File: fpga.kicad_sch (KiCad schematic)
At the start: 12 parts, among them U11 TLV77512PDBVR, U12 TLV77525PDBVR, U13 TLV77533PDBVR, U2 ICE40LP1K-CM36

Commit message: More re-layout for the new design
Signed-off-by: Corey Minyard <corey@minyard.net>
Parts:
- added R34, R35, R36: 10K, Resistor_SMD:R_0402_1005Metric, symbol Device:R
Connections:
- net +3.3V: now also U11.3 (ON/~{OFF}), R36.2
- net 144MHz_TX_ENABLE: now also U2.A1 (IOL_2B)
- net 144_SWITCH: now also U2.A2 (IOT_89)
- net 440MHz_TX_ENABLE: now also U2.B5 (IOR_63)
- net 440_SWITCH: now also U2.B4 (IOR_61_GBIN2)
- net FPGA_3.3V: now also R35.2
- net FPGA_SPI_SSEL: now also U2.D5 (IOB_47_SS), R34.2
- net GND: now also R34.1
- net RADIO2_RESET_N: now also U2.B6 (IOR_64)
- net RADIO_SPI_MISO: now also U2.E4 (IOB_44_SDO)
- net RADIO_SPI_MOSI: now also U2.F5 (IOB_45_SDI)
- net RADIO_SPI_SCLK: now also U2.E5 (IOB_46_SCK)
- net TX_144_ON: now also U2.A3 (IOT_84_GBIN1)
- net TX_440_ON: now also U2.B3 (IOT_85_GBIN0)
- net RADIO1_GPIO0: now reaches U2.B1 (IOL_2A)
- net RADIO1_GPIO2: now reaches U2.C1 (IOL_6B_GBIN7)
- net FPGA_CDONE/IRQ_N: now reaches U2.C3 (IOT_90)
- net FPGA_CDONE/IRQ_N: now also U2.C4 (CDONE), R36.1
- net RADIO2_GPIO3: now reaches U2.C6 (IOR_65)
- net RADIO1_GPIO3: now reaches U2.D1 (IOL_7A_GBIN6)
- net RADIO2_GPIO2: now reaches U2.D6 (IOR_55)
- net RADIO1_RESET_N: now reaches U2.E1 (IOL_7B)
- net RADIO2_GPIO0: now reaches U2.E6 (IOR_54)
- net FPGA_RESET_N: now reaches U2.F4 (CRESET_B)
- net FPGA_RESET_N: now also R35.1
- no-connect marks 2 -> 7
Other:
- moved on the sheet: U2

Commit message: Finish initial layet
Signed-off-by: Corey Minyard <corey@minyard.net>
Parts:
- added R37, R38: 0, Resistor_SMD:R_0402_1005Metric, symbol Device:R
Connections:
- net at U2.C2 (IOL_6A): now also R37.2
- net at U2.F3 (IOB_43_CBSEL1): now also R38.2
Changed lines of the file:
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@@
-	)
-	(no_connect
-		(at 187.96 49.53)
 	)
 	(no_connect
@@
 	)
 	(no_connect
+		(at 240.03 95.25)
+	)
+	(no_connect
+		(at 240.03 49.53)
+	)
+	(no_connect
 		(at 187.96 64.77)
 	)
@@
 		(at 96.52 44.45)
 	)
-	(no_connect
-		(at 187.96 95.25)
-	)
 	(wire
 		(pts
@@
 	(wire
 		(pts
+			(xy 187.96 49.53) (xy 232.41 49.53)
+		)
+		(stroke
+			(width 0)
+			(type default)
+		)
+	)
+	(wire
+		(pts
 			(xy 187.96 57.15) (xy 208.28 57.15)
 		)
@@
 		(pts
 			(xy 20.32 67.31) (xy 20.32 137.16)
+		)
+		(stroke
+			(width 0)
+			(type default)
+		)
+	)
+	(wire
+		(pts
+			(xy 187.96 95.25) (xy 232.41 95.25)
 		)
 		(stroke
@@
 	)
 	(symbol
+		(lib_id "Device:R")
+		(at 236.22 49.53 270)
+		(unit 1)
+		(exclude_from_sim no)
+		(in_bom no)
+		(on_board yes)
+		(dnp yes)
+		(property "Reference" "R38"
+			(at 241.046 51.054 90)
+			(effects
+				(font
+					(size 1.27 1.27)
+				)
+			)
+		)
+		(property "Value" "0"
+			(at 232.156 50.546 90)
+			(effects
+				(font
+					(size 1.27 1.27)
+				)
+			)
+		)
+		(property "Footprint" "Resistor_SMD:R_0402_1005Metric"
+			(at 236.22 47.752 90)
+			(effects
+				(font
+					(size 1.27 1.27)
+				)
+				(hide yes)
+			)
+		)
+		(property "Datasheet" "~"
+			(at 236.22 49.53 0)
+			(effects
+				(font
+					(size 1.27 1.27)
+				)
+				(hide yes)
+			)
+		)
+		(property "Description" "Resistor"
+			(at 236.22 49.53 0)
+			(effects
+				(font
+					(size 1.27 1.27)
+				)
+				(hide yes)
+			)
+		)
+		(pin "2"
+		)
+		(pin "1"
+		)
+		(instances
+			(project "FSKGroundStation"
+				(path "/23e49ab9-97e0-460a-806c-ff6f37958474/a7d34897-eb3f-4db7-9b4e-9397ce1d9e5d"
+					(reference "R38")
+					(unit 1)
+				)
+			)
+		)
+	)
+	(symbol
 		(lib_id "Local ICs:TLV775 3.3V")
 		(at 45.72 100.33 0)
@@
 		(on_board yes)
 		(dnp no)
-		(fields_autoplaced yes)
 		(property "Reference" "#PWR0147"
 			(at 236.22 92.71 0)
@@
 		)
 		(property "Value" "GND"
-			(at 236.22 91.44 0)
+			(at 236.22 90.17 0)
 			(effects
 				(font
@@
 					(unit 1)
 				)
+			)
+		)
+	)
+	(symbol
+		(lib_id "Device:R")
+		(at 236.22 95.25 270)
+		(unit 1)
+		(exclude_from_sim no)
+		(in_bom no)
+		(on_board yes)
+		(dnp yes)
+		(property "Reference" "R37"
+			(at 236.474 98.044 90)
+			(effects
+				(font
+					(size 1.27 1.27)
+				)
+			)
+		)
+		(property "Value" "0"
+			(at 236.22 92.71 90)
+			(effects
+				(font
+					(size 1.27 1.27)
+				)
+			)
+		)
+		(property "Footprint" "Resistor_SMD:R_0402_1005Metric"
+			(at 236.22 93.472 90)
+			(effects
+				(font
+					(size 1.27 1.27)
+				)
+				(hide yes)
+			)
+		)
+		(property "Datasheet" "~"
+			(at 236.22 95.25 0)
+			(effects
+				(font
+					(size 1.27 1.27)
+				)
+				(hide yes)
+			)
+		)
+		(property "Description" "Resistor"
+			(at 236.22 95.25 0)
+			(effects
+				(font
+					(size 1.27 1.27)
+				)
+				(hide yes)
+			)
+		)
+		(pin "2"
+		)
+		(pin "1"
+		)
+		(instances
+			(project "FSKGroundStation"
+				(path "/23e49ab9-97e0-460a-806c-ff6f37958474/a7d34897-eb3f-4db7-9b4e-9397ce1d9e5d"
+					(reference "R37")
+					(unit 1)
+				)

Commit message: Add some LEDs
Signed-off-by: Corey Minyard <corey@minyard.net>
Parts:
- added D3: RED LED, LED_SMD:LED_0603_1608Metric_Pad1.05x0.95mm_HandSolder, symbol Device:LED
- added D5: GREEN LED, LED_SMD:LED_0603_1608Metric_Pad1.05x0.95mm_HandSolder, symbol Device:LED
- R37, R38: value 0 -> 3KΩ; footprint Resistor_SMD:R_0402_1005Metric -> Resistor_SMD:R_0603_1608Metric_Pad0.98x0.95mm_HandSolder; now fitted; now in the parts list
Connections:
- net +3.3V: now also D3.2 (A), D5.2 (A)
- net at R38.1: now also D5.1 (K)
- net at R37.1: now also D3.1 (K)
- no-connect marks 7 -> 5

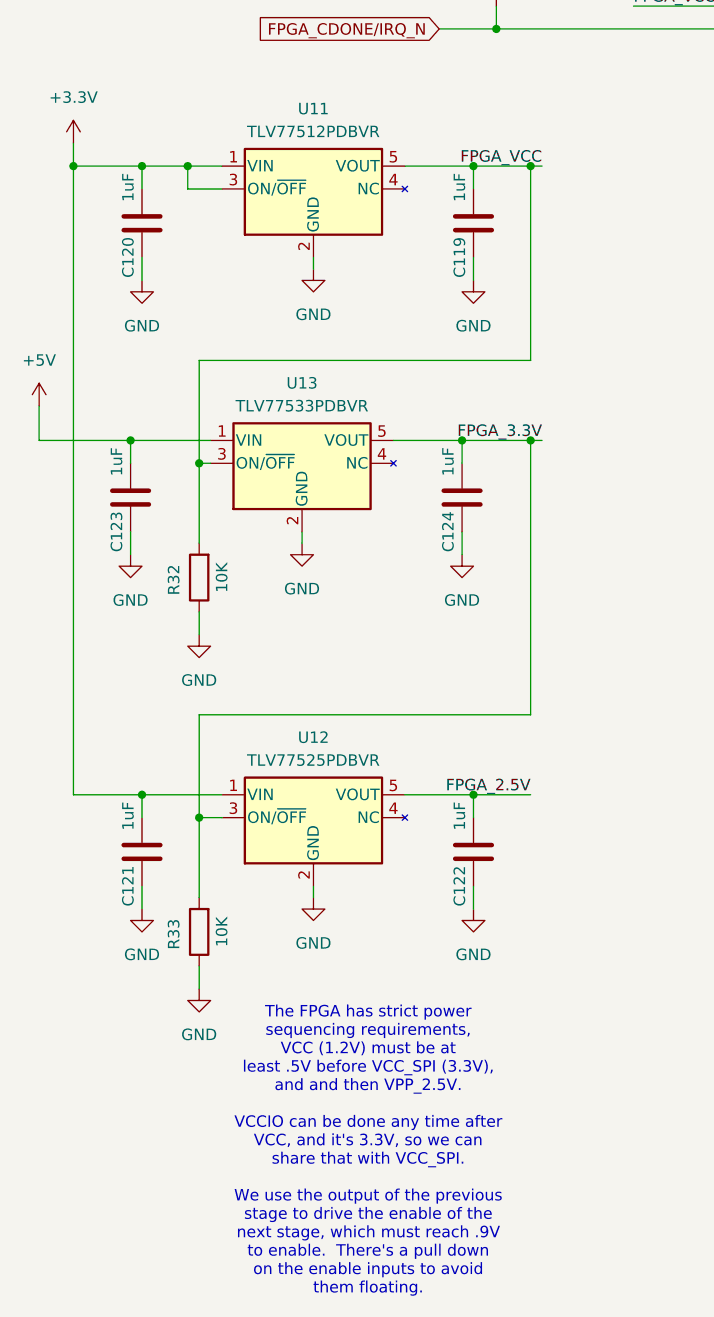
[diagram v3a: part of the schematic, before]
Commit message: Use a diode to provide the 2.5V voltage for the FPGA
Drops 3.3V down to 2.8V, which is in range.  It's a lot simpler.

Also do some via cleanup.

Signed-off-by: Corey Minyard <corey@minyard.net>
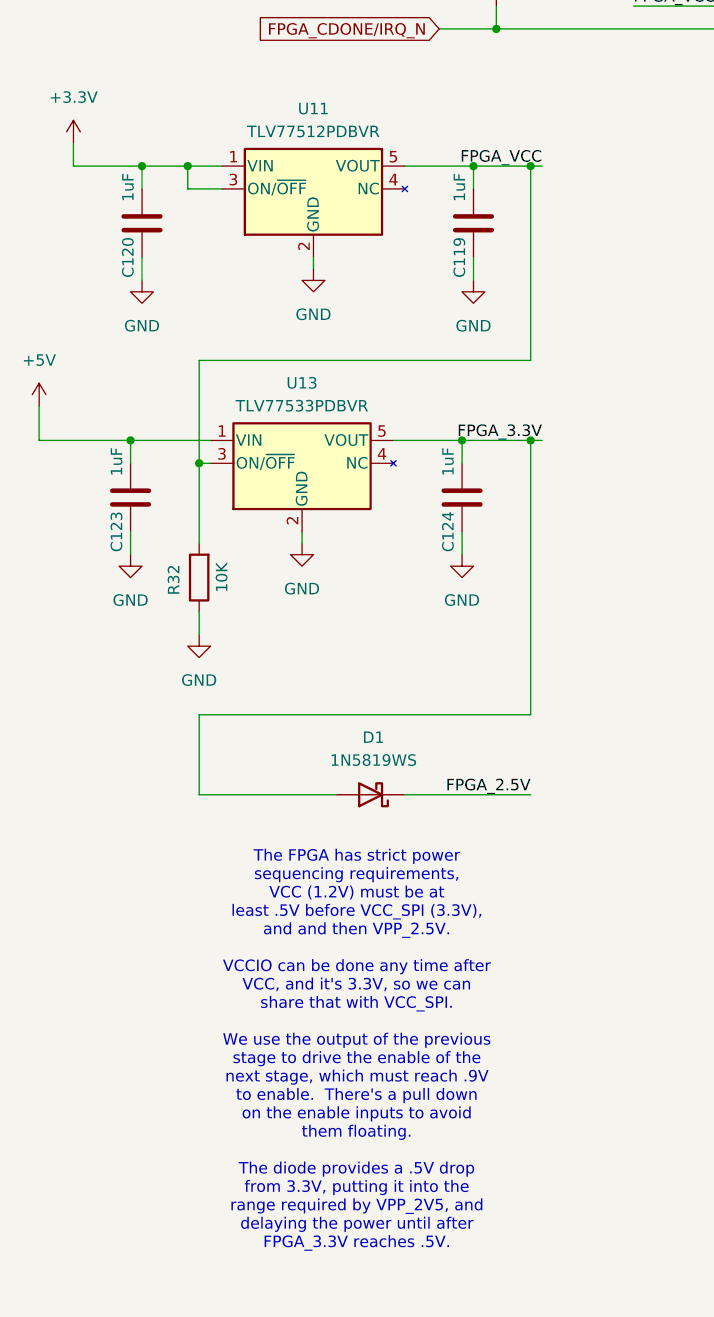
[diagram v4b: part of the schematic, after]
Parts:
- removed C121, C122: 1uF, Capacitor_SMD:C_0603_1608Metric_Pad1.08x0.95mm_HandSolder, symbol Device:C
- removed R33: 10K, Resistor_SMD:R_0402_1005Metric, symbol Device:R
- removed U12: TLV77525PDBVR, Package_TO_SOT_SMD:SOT-23-5, symbol Local ICs:TLV775 2.5V
- added D1: 1N5819WS, Diode_SMD:D_SOD-323, symbol Diode:1N5819WS
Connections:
- net FPGA_2.5V: now also D1.1 (K)
- net FPGA_3.3V: now also D1.2 (A)
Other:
- note added: "The FPGA has strict power sequencing requirements, VCC (1.2V) must be at least .5V before VCC_SPI (3.3V), and and then VPP_2.5V. VCCIO can be done any time after VCC, and it's 3.3V, so we can share that with VCC_SPI. We use the output of the previous stage to drive the enable of the next stage, which must reach .9V to enable. There's a pull down on the enable inputs to avoid them floating. The di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"
- note removed: "The FPGA has strict power sequencing requirements, VCC (1.2V) must be at least .5V before VCC_SPI (3.3V), and and then VPP_2.5V. VCCIO can be done any time after VCC, and it's 3.3V, so we can share that with VCC_SPI. We use the output of the previous stage to drive the enable of the next stage, which must reach .9V to enable. There's a pull down on the enable inputs to avoid them floating."

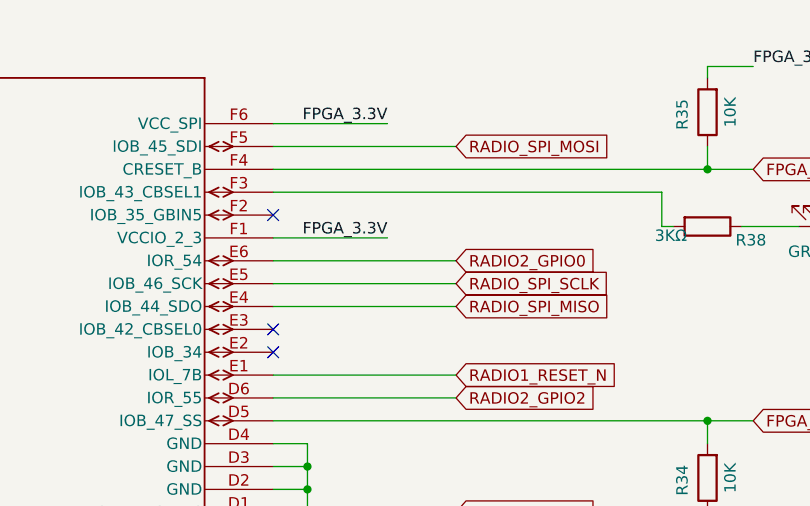
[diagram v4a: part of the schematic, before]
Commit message: Add a DNP resistor on an FPGA pin
Make it available for use.  Clean up routing around the FPGA a bit, too.

Signed-off-by: Corey Minyard <corey@minyard.net>
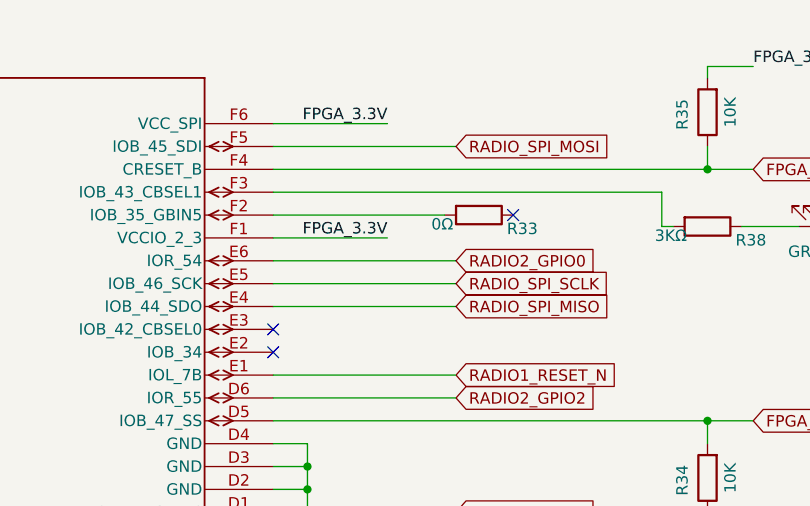
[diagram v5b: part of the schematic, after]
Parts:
- added R33: 0Ω, Resistor_SMD:R_0402_1005Metric_Pad0.72x0.64mm_HandSolder, symbol Device:R
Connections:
- net at U2.F2 (IOB_35_GBIN5): now also R33.2
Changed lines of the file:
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@@
-	)
-	(no_connect
-		(at 187.96 52.07)
 	)
 	(no_connect
@@
 	)
 	(no_connect
+		(at 214.63 52.07)
+	)
+	(no_connect
 		(at 187.96 64.77)
 	)
@@
 		(pts
 			(xy 34.29 128.27) (xy 34.29 137.16)
+		)
+		(stroke
+			(width 0)
+			(type default)
+		)
+	)
+	(wire
+		(pts
+			(xy 187.96 52.07) (xy 207.01 52.07)
 		)
 		(stroke
@@
 					(unit 1)
 				)
+			)
+		)
+	)
+	(symbol
+		(lib_id "Device:R")
+		(at 210.82 52.07 270)
+		(unit 1)
+		(exclude_from_sim no)
+		(in_bom yes)
+		(on_board yes)
+		(dnp no)
+		(property "Reference" "R33"
+			(at 215.646 53.594 90)
+			(effects
+				(font
+					(size 1.27 1.27)
+				)
+			)
+		)
+		(property "Value" "0Ω"
+			(at 206.756 53.086 90)
+			(effects
+				(font
+					(size 1.27 1.27)
+				)
+			)
+		)
+		(property "Footprint" "Resistor_SMD:R_0402_1005Metric_Pad0.72x0.64mm_HandSolder"
+			(at 210.82 50.292 90)
+			(effects
+				(font
+					(size 1.27 1.27)
+				)
+				(hide yes)
+			)
+		)
+		(property "Datasheet" "~"
+			(at 210.82 52.07 0)
+			(effects
+				(font
+					(size 1.27 1.27)
+				)
+				(hide yes)
+			)
+		)
+		(property "Description" "Resistor"
+			(at 210.82 52.07 0)
+			(effects
+				(font
+					(size 1.27 1.27)
+				)
+				(hide yes)
+			)
+		)
+		(pin "2"
+		)
+		(pin "1"
+		)
+		(instances
+			(project "FSKGroundStation"
+				(path "/23e49ab9-97e0-460a-806c-ff6f37958474/a7d34897-eb3f-4db7-9b4e-9397ce1d9e5d"
+					(reference "R33")
+					(unit 1)
+				)

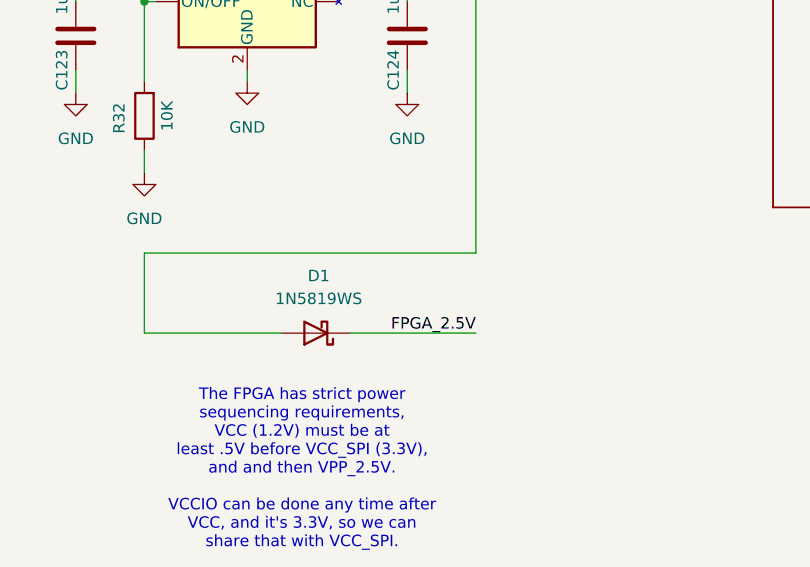
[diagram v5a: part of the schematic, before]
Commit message: Switch to a CPU with a USB interface for the USB connection
The part that was picked had proprietary tools and configuration and it
didn't support interrupts.  The CPU is cheaper and more capable.

Signed-off-by: Corey Minyard <corey@minyard.net>
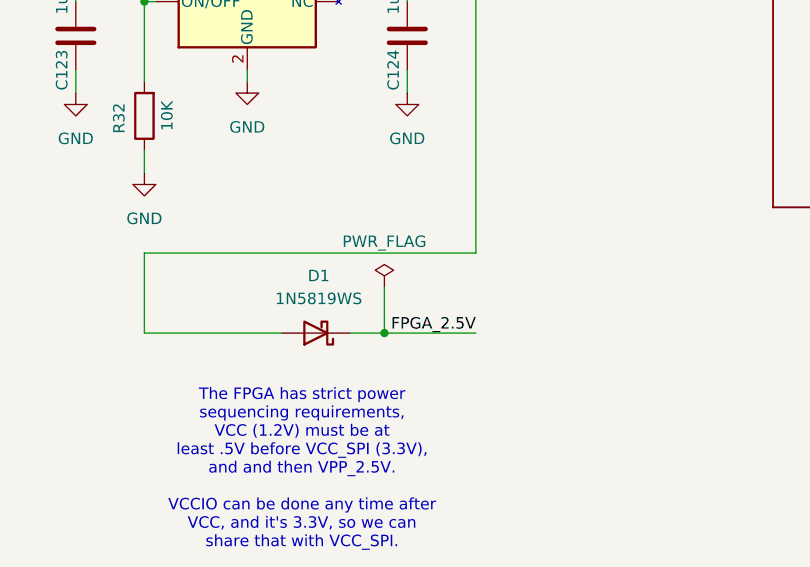
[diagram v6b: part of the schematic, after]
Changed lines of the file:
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@@
+	)
+	(junction
+		(at 60.96 137.16)
+		(diameter 0)
+		(color 0 0 0 0)
 	)
 	(junction
@@
 	(wire
 		(pts
-			(xy 57.15 137.16) (xy 71.12 137.16)
+			(xy 57.15 137.16) (xy 60.96 137.16)
 		)
 		(stroke
@@
 		(pts
 			(xy 82.55 41.91) (xy 96.52 41.91)
+		)
+		(stroke
+			(width 0)
+			(type default)
+		)
+	)
+	(wire
+		(pts
+			(xy 60.96 137.16) (xy 71.12 137.16)
+		)
+		(stroke
+			(width 0)
+			(type default)
+		)
+	)
+	(wire
+		(pts
+			(xy 60.96 132.08) (xy 60.96 137.16)
 		)
 		(stroke
@@
 					(unit 1)
 				)
+			)
+		)
+	)
+	(symbol
+		(lib_id "power:PWR_FLAG")
+		(at 60.96 132.08 0)
+		(unit 1)
+		(exclude_from_sim no)
+		(in_bom yes)
+		(on_board yes)
+		(dnp no)
+		(fields_autoplaced yes)
+		(property "Reference" "#FLG05"
+			(at 60.96 130.175 0)
+			(effects
+				(font
+					(size 1.27 1.27)
+				)
+				(hide yes)
+			)
+		)
+		(property "Value" "PWR_FLAG"
+			(at 60.96 127 0)
+			(effects
+				(font
+					(size 1.27 1.27)
+				)
+			)
+		)
+		(property "Footprint" ""
+			(at 60.96 132.08 0)
+			(effects
+				(font
+					(size 1.27 1.27)
+				)
+				(hide yes)
+			)
+		)
+		(property "Datasheet" "~"
+			(at 60.96 132.08 0)
+			(effects
+				(font
+					(size 1.27 1.27)
+				)
+				(hide yes)
+			)
+		)
+		(property "Description" "Special symbol for telling ERC where power comes from"
+			(at 60.96 132.08 0)
+			(effects
+				(font
+					(size 1.27 1.27)
+				)
+				(hide yes)
+			)
+		)
+		(pin "1"
+		)
+		(instances
+			(project "FSKGroundStation"
+				(path "/23e49ab9-97e0-460a-806c-ff6f37958474/a7d34897-eb3f-4db7-9b4e-9397ce1d9e5d"
+					(reference "#FLG05")
+					(unit 1)
+				)

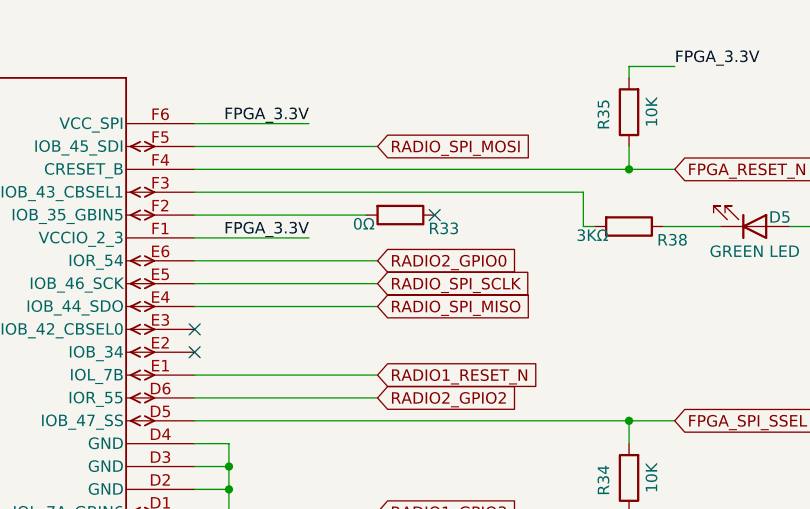
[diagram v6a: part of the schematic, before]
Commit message: Add a clock from the USB chip to the FPGA
The FPGA might need a clock for certain things, so provide it.

Signed-off-by: Corey Minyard <corey@minyard.net>
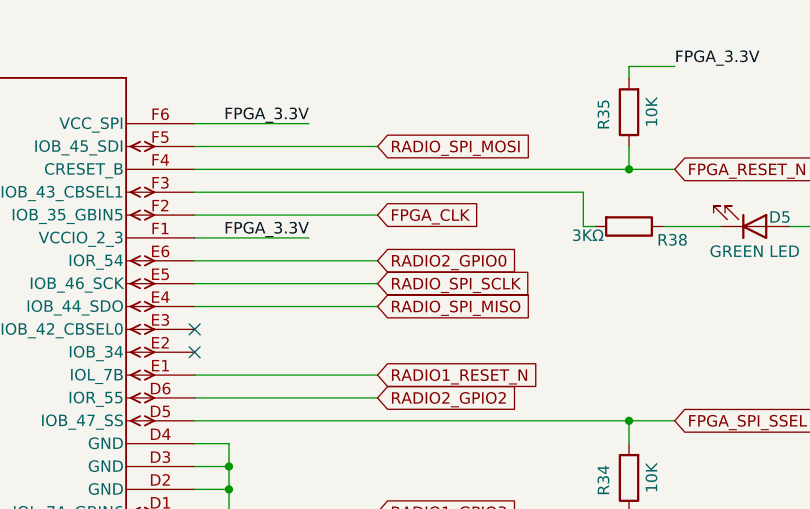
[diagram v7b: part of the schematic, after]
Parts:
- removed R33: 0Ω, Resistor_SMD:R_0402_1005Metric_Pad0.72x0.64mm_HandSolder, symbol Device:R
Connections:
- net FPGA_CLK: now reaches U2.F2 (IOB_35_GBIN5)
- no-connect marks 5 -> 4
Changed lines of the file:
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@@
-	)
-	(no_connect
-		(at 214.63 52.07)
 	)
 	(no_connect
@@
 	(wire
 		(pts
-			(xy 187.96 52.07) (xy 207.01 52.07)
+			(xy 187.96 52.07) (xy 208.28 52.07)
 		)
 		(stroke
@@
 		(property "Intersheetrefs" "${INTERSHEET_REFS}"
 			(at 258.618 74.93 0)
+			(effects
+				(font
+					(size 1.27 1.27)
+				)
+				(justify left)
+				(hide yes)
+			)
+		)
+	)
+	(global_label "FPGA_CLK"
+		(shape input)
+		(at 208.28 52.07 0)
+		(fields_autoplaced yes)
+		(effects
+			(font
+				(size 1.27 1.27)
+			)
+			(justify left)
+		)
+		(property "Intersheetrefs" "${INTERSHEET_REFS}"
+			(at 220.5181 52.07 0)
 			(effects
 				(font
@@
 		)
 		(property "Value" "3KΩ"
-			(at 232.156 54.356 90)
+			(at 231.648 54.356 90)
 			(effects
 				(font
@@
 					(unit 1)
 				)
-			)
-		)
-	)
-	(symbol
-		(lib_id "Device:R")
-		(at 210.82 52.07 270)
-		(unit 1)
-		(exclude_from_sim no)
-		(in_bom yes)
-		(on_board yes)
-		(dnp no)
-		(property "Reference" "R33"
-			(at 215.646 53.594 90)
-			(effects
-				(font
-					(size 1.27 1.27)
-				)
-			)
-		)
-		(property "Value" "0Ω"
-			(at 206.756 53.086 90)
-			(effects
-				(font
-					(size 1.27 1.27)
-				)
-			)
-		)
-		(property "Footprint" "Resistor_SMD:R_0402_1005Metric_Pad0.72x0.64mm_HandSolder"
-			(at 210.82 50.292 90)
-			(effects
-				(font
-					(size 1.27 1.27)
-				)
-				(hide yes)
-			)
-		)
-		(property "Datasheet" "~"
-			(at 210.82 52.07 0)
-			(effects
-				(font
-					(size 1.27 1.27)
-				)
-				(hide yes)
-			)
-		)
-		(property "Description" "Resistor"
-			(at 210.82 52.07 0)
-			(effects
-				(font
-					(size 1.27 1.27)
-				)
-				(hide yes)
-			)
-		)
-		(pin "2"
-		)
-		(pin "1"
-		)
-		(instances
-			(project "FSKGroundStation"
-				(path "/23e49ab9-97e0-460a-806c-ff6f37958474/a7d34897-eb3f-4db7-9b4e-9397ce1d9e5d"
-					(reference "R33")
-					(unit 1)
-				)
